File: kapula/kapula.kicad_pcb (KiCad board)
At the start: 4 copper layers, 50 x 59 mm, 161 parts, among them J1 Conn_02x10_Odd_Even, J12 U.FL, J13 U.FL, J3 Conn_02x10_Odd_Even, J4 Conn_ARM_JTAG_SWD_10, J5 U.FL, J9 U.FL, Q1 AO3401A, Q2 AO3401A, Q3 AO3400A, Q4 BSS84, Q5 AO3400A, Q6 AO3400A, T1 BW21S7511A01TF, T2 BW21S7511A01TF, T3 BW21S7511A01TF, T4 BW21S7511A01TF, U1 XC6206P332MR, U2 TP4054, U3 DW01+G, U5 EFR32FG14P233F256GM48-B, U6 XA213-G4J, X1 DSB221SDN, Y1 32768 Hz

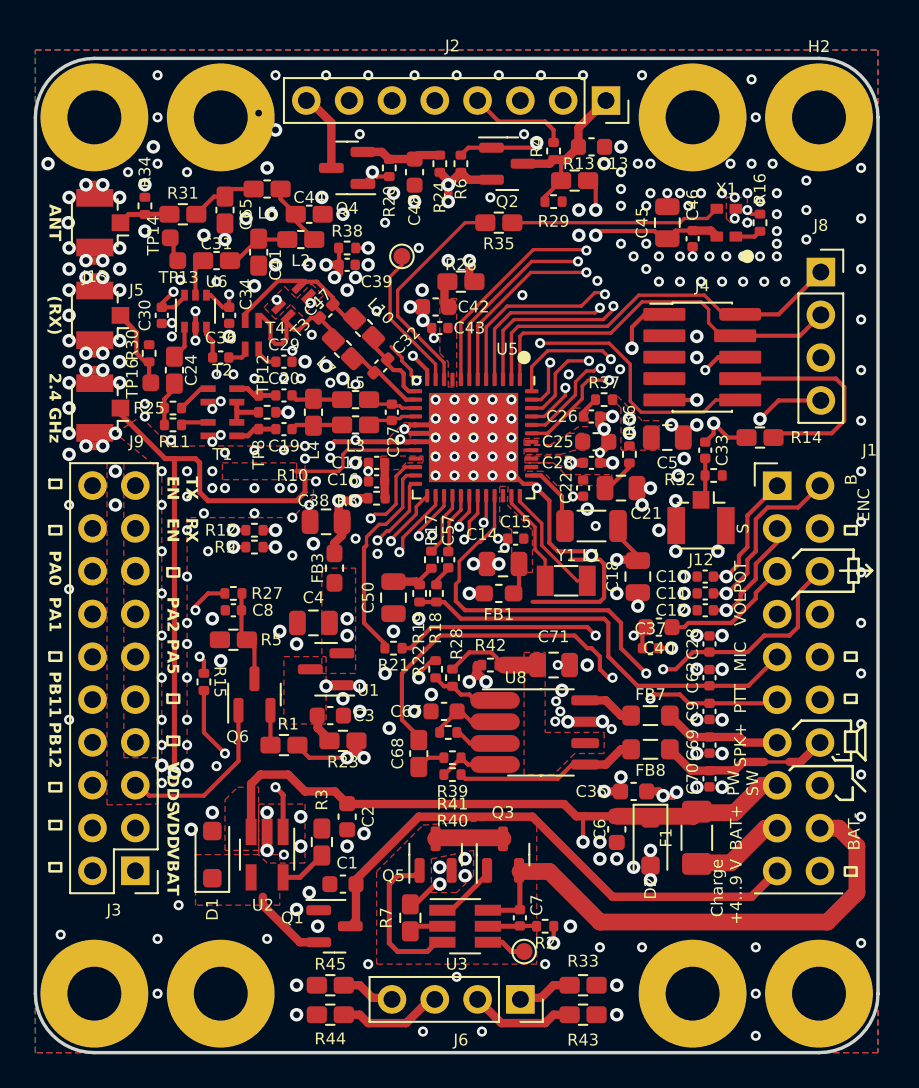
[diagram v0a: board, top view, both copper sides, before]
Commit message: PCB: Add more silkscreen texts, some other fixes
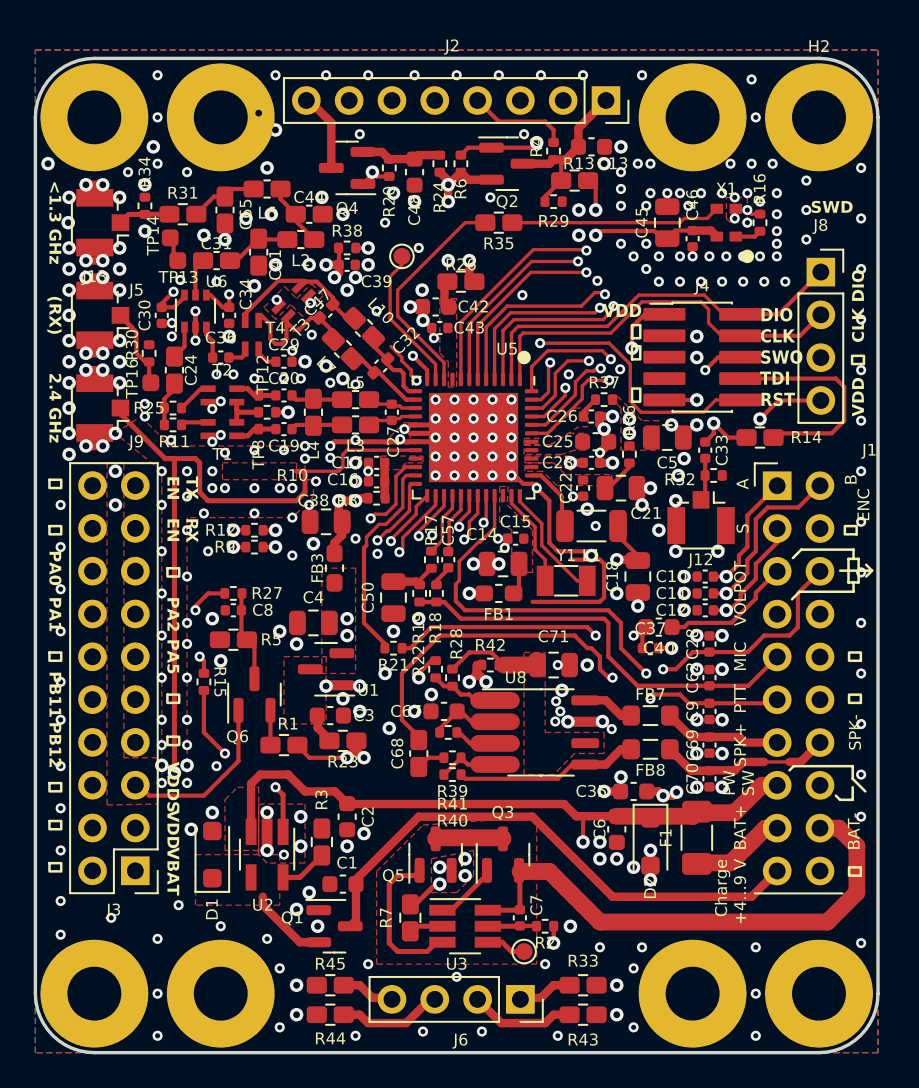
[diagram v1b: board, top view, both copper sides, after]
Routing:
- net GND: vias 368 -> 384
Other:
- board text added: "<1.3 GHz"
- board text added: "DIO CLK SWO TDI RST"
- board text added: "SPK-"
- board text added: "SWD"
- board text added: "VDD ⏚ CLK DIO"
- board text added: "VDD ⏚ ⏚ ⏚"
- board text removed: "ANT"

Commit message: PCB: Small circuit changes and layout improvements
* Add pads for extra series resistor for backlight
* Improve 2nd harmonic rejection of lowpass filter
* Move some components and vias a bit
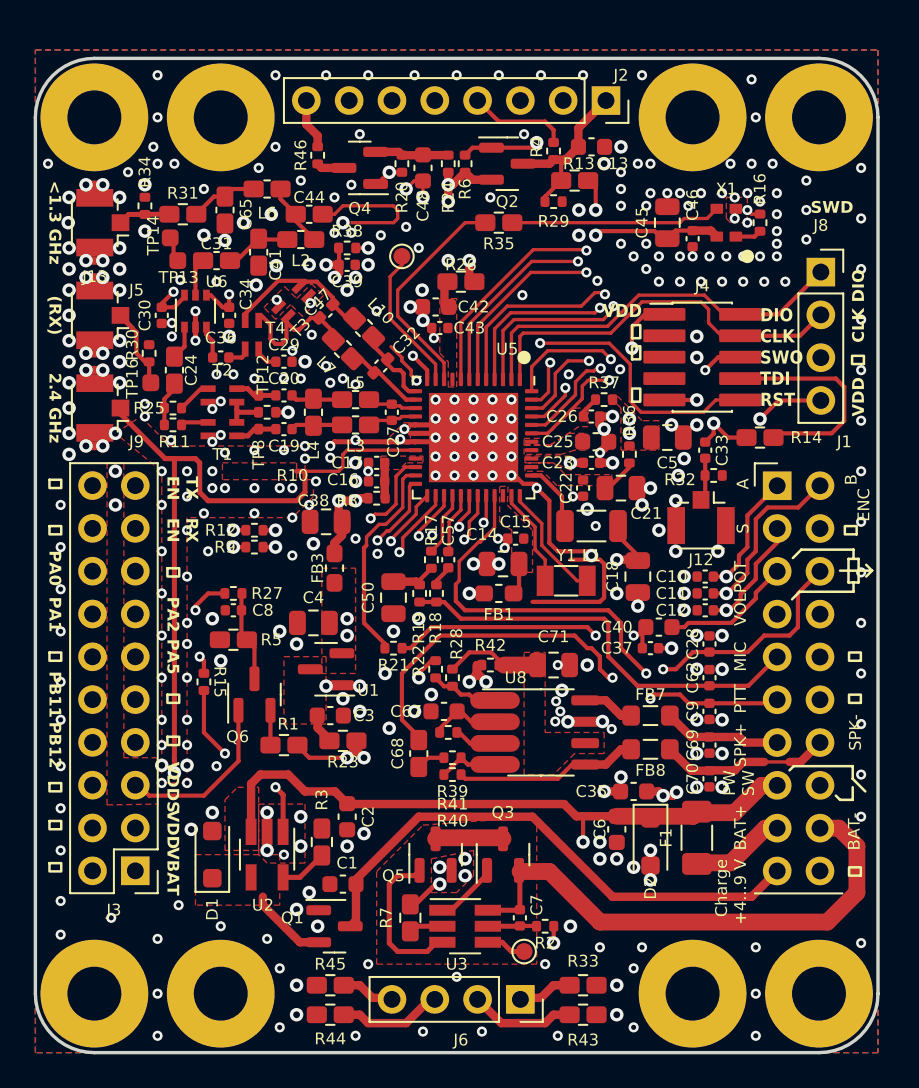
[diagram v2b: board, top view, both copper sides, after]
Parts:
- added NT2: ~, kapula:NetTie-2_SMD_Pad0.2mm, F.Cu at (119.0, 67.2)
- added R46: 0, Resistor_SMD:R_0402_1005Metric, F.Cu at (116.8, 63.2)
- C44: value 10p -> 8p2
- moved R20 0.79 mm to (121.8, 63.8)
- moved Q4 0.75 mm to (119.2, 64.0)
- moved C48 0.56 mm to (123.0, 64.0)
- moved R24 0.50 mm to (124.5, 63.8)
- moved R6 0.25 mm to (125.5, 63.8)
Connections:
- C44 pad 2: GND -> Net-(C44-Pad2)
- Q4 pad 3: /D_LED -> Net-(Q4-D)
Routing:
- net Net-(C44-Pad2): track 0.00 -> 7.61 mm
- net GND: track 66.6 -> 68.7 mm, vias 384 -> 389
- net Net-(Q4-D): track 0.00 -> 1.66 mm
- net /D_LED: track 4.71 -> 3.19 mm
- net /~{D_LED_EN}: track 26.3 -> 25.2 mm

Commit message: PCB: Fix inductor value in lowpass filter
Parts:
- L2, L6: value 22n -> 18n
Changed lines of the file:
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@@
     (descr "Inductor SMD 0603 (1608 Metric), square (rectangular) end terminal, IPC_7351 nominal with elongated pad for handsoldering. (Body size source: http://www.tortai-tech.com/upload/download/2011102023233369053.pdf), generated with kicad-footprint-generator")
     (tags "inductor handsolder")
-    (property "LCSC" "C12099")
+    (property "LCSC" "C48590")
     (property "Sheetfile" "kapula.kicad_sch")
     (property "Sheetname" "")
@@
         (effects (font (size 0.7 0.7) (thickness 0.15)))
     )
-    (fp_text value "22n" (at 0 1.43) (layer "F.Fab")
+    (fp_text value "18n" (at 0 1.43) (layer "F.Fab")
         (effects (font (size 1 1) (thickness 0.15)))
     )
@@
     (descr "Inductor SMD 0603 (1608 Metric), square (rectangular) end terminal, IPC_7351 nominal with elongated pad for handsoldering. (Body size source: http://www.tortai-tech.com/upload/download/2011102023233369053.pdf), generated with kicad-footprint-generator")
     (tags "inductor handsolder")
-    (property "LCSC" "C12099")
+    (property "LCSC" "C48590")
     (property "Sheetfile" "kapula.kicad_sch")
     (property "Sheetname" "")
@@
         (effects (font (size 0.7 0.7) (thickness 0.15)))
     )
-    (fp_text value "22n" (at 0 1.43) (layer "F.Fab")
-        (effects (font (size 1 1) (thickness 0.15)))
-    )
+    (fp_text value "18n" (at 0 1.43) (layer "F.Fab")
+        (effects (font (size 1 1) (thickness 0.15)))
+    )

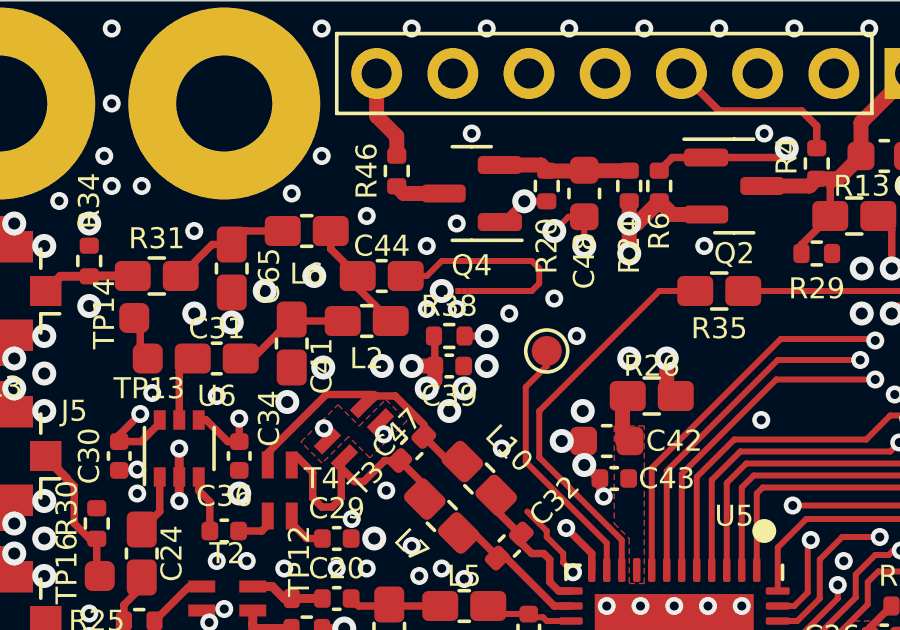
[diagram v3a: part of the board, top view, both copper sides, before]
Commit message: PCB: Modify lowpass to use inductors from JLC basic series
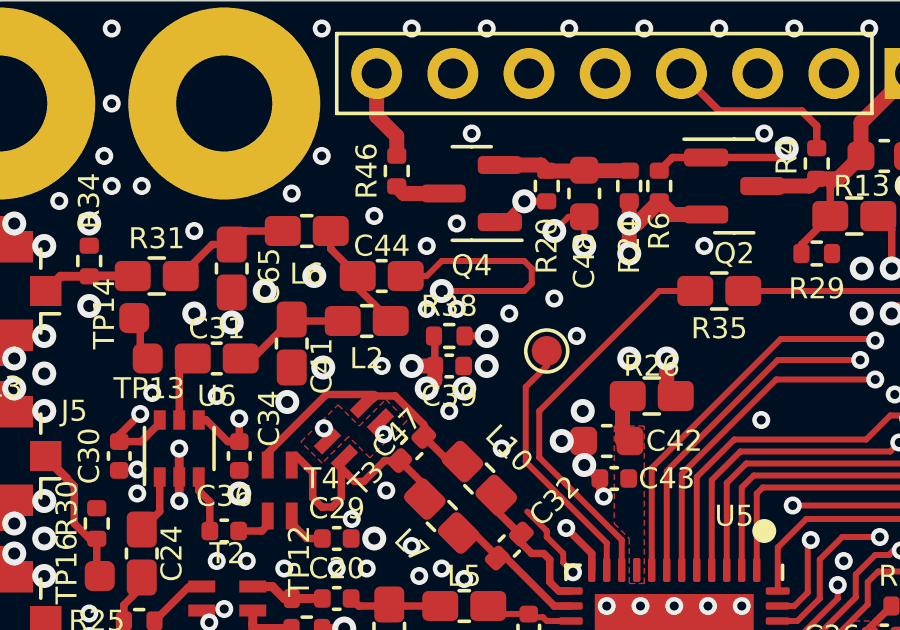
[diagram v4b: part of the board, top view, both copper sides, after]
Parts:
- C41, C65: value 4p7 -> 6p8
- C44: value 8p2 -> 10p
- L2, L6: value 18n -> 15n
- moved NT2 0.25 mm to (118.8, 67.2)
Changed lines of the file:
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@@
     (descr "Inductor SMD 0603 (1608 Metric), square (rectangular) end terminal, IPC_7351 nominal with elongated pad for handsoldering. (Body size source: http://www.tortai-tech.com/upload/download/2011102023233369053.pdf), generated with kicad-footprint-generator")
     (tags "inductor handsolder")
-    (property "LCSC" "C48590")
+    (property "LCSC" "C27143")
     (property "Sheetfile" "kapula.kicad_sch")
     (property "Sheetname" "")
@@
         (effects (font (size 0.7 0.7) (thickness 0.15)))
     )
-    (fp_text value "18n" (at 0 1.43) (layer "F.Fab")
+    (fp_text value "15n" (at 0 1.43) (layer "F.Fab")
         (effects (font (size 1 1) (thickness 0.15)))
     )
@@
     (descr "Inductor SMD 0603 (1608 Metric), square (rectangular) end terminal, IPC_7351 nominal with elongated pad for handsoldering. (Body size source: http://www.tortai-tech.com/upload/download/2011102023233369053.pdf), generated with kicad-footprint-generator")
     (tags "inductor handsolder")
-    (property "LCSC" "C48590")
+    (property "LCSC" "C27143")
     (property "Sheetfile" "kapula.kicad_sch")
     (property "Sheetname" "")
@@
         (effects (font (size 0.7 0.7) (thickness 0.15)))
     )
-    (fp_text value "18n" (at 0 1.43) (layer "F.Fab")
+    (fp_text value "15n" (at 0 1.43) (layer "F.Fab")
         (effects (font (size 1 1) (thickness 0.15)))
     )
@@
     (descr "Capacitor SMD 0603 (1608 Metric), square (rectangular) end terminal, IPC_7351 nominal with elongated pad for handsoldering. (Body size source: IPC-SM-782 page 76, https://www.pcb-3d.com/wordpress/wp-content/uploads/ipc-sm-782a_amendment_1_and_2.pdf), generated with kicad-footprint-generator")
     (tags "capacitor handsolder")
-    (property "LCSC" "C1569")
+    (property "LCSC" "C1679")
     (property "Sheetfile" "kapula.kicad_sch")
     (property "Sheetname" "")
@@
         (effects (font (size 0.7 0.7) (thickness 0.15)))
     )
-    (fp_text value "4p7" (at 0 1.43 90) (layer "F.Fab")
+    (fp_text value "6p8" (at 0 1.43 90) (layer "F.Fab")
         (effects (font (size 1 1) (thickness 0.15)))
     )
@@
     (descr "Capacitor SMD 0603 (1608 Metric), square (rectangular) end terminal, IPC_7351 nominal with elongated pad for handsoldering. (Body size source: IPC-SM-782 page 76, https://www.pcb-3d.com/wordpress/wp-content/uploads/ipc-sm-782a_amendment_1_and_2.pdf), generated with kicad-footprint-generator")
     (tags "capacitor handsolder")
-    (property "LCSC" "C1569")
+    (property "LCSC" "C1679")
     (property "Sheetfile" "kapula.kicad_sch")
     (property "Sheetname" "")
@@
         (effects (font (size 0.7 0.7) (thickness 0.15)))
     )
-    (fp_text value "4p7" (at 0 1.43 90) (layer "F.Fab")
+    (fp_text value "6p8" (at 0 1.43 90) (layer "F.Fab")
         (effects (font (size 1 1) (thickness 0.15)))
     )
@@
   )
   (footprint "kapula:NetTie-2_SMD_Pad0.2mm" (layer "F.Cu")
-    (at 119 67.25 180)
+    (at 118.75 67.25 180)
     (descr "Net tie, 2 pin, 0.5mm square SMD pads")
     (tags "net tie")
@@
     (descr "Capacitor SMD 0603 (1608 Metric), square (rectangular) end terminal, IPC_7351 nominal with elongated pad for handsoldering. (Body size source: IPC-SM-782 page 76, https://www.pcb-3d.com/wordpress/wp-content/uploads/ipc-sm-782a_amendment_1_and_2.pdf), generated with kicad-footprint-generator")
     (tags "capacitor handsolder")
-    (property "LCSC" "C1685")
+    (property "LCSC" "C1634")
     (property "Sheetfile" "kapula.kicad_sch")
     (property "Sheetname" "")
@@
         (effects (font (size 0.7 0.7) (thickness 0.15)))
     )
-    (fp_text value "8p2" (at 0 1.43) (layer "F.Fab")
+    (fp_text value "10p" (at 0 1.43) (layer "F.Fab")
         (effects (font (size 1 1) (thickness 0.15)))
     )
@@
   (via (at 114.75 76.5) (size 0.6) (drill 0.3) (layers "F.Cu" "B.Cu") (free) (net 2))
   (via (at 140 69.25) (size 0.6) (drill 0.3) (layers "F.Cu" "B.Cu") (free) (net 2))
-  (via (at 116.25 69.75) (size 0.8) (drill 0.4) (layers "F.Cu" "B.Cu") (free) (net 2))
+  (via (at 116.25 69.75) (size 0.6) (drill 0.3) (layers "F.Cu" "B.Cu") (free) (net 2))
   (via (at 134.7 75.95) (size 0.6) (drill 0.3) (layers "F.Cu" "B.Cu") (free) (net 2))
   (via (at 136 58.5) (size 0.6) (drill 0.3) (layers "F.Cu" "B.Cu") (free) (net 2))
@@
   (via (at 143.75 63.75) (size 0.6) (drill 0.3) (layers "F.Cu" "B.Cu") (free) (net 2))
   (via (at 119 76.85) (size 0.6) (drill 0.3) (layers "F.Cu" "B.Cu") (free) (net 2))
-  (via (at 118.5 71.25) (size 0.8) (drill 0.4) (layers "F.Cu" "B.Cu") (free) (net 2))
+  (via (at 118.5 71.25) (size 0.6) (drill 0.3) (layers "F.Cu" "B.Cu") (free) (net 2))
   (via (at 110.25 86.75) (size 0.6) (drill 0.3) (layers "F.Cu" "B.Cu") (free) (net 2))
   (via (at 136.25 68.5) (size 0.6) (drill 0.3) (layers "F.Cu" "B.Cu") (free) (net 2))
@@
   (via (at 119 70.5) (size 0.8) (drill 0.4) (layers "F.Cu" "B.Cu") (free) (net 2))
   (via (at 134.75 100.15) (size 0.8) (drill 0.4) (layers "F.Cu" "B.Cu") (free) (net 2))
-  (via (at 115.75 64.75) (size 0.6) (drill 0.3) (layers "F.Cu" "B.Cu") (free) (net 2))
+  (via (at 116 64.75) (size 0.6) (drill 0.3) (layers "F.Cu" "B.Cu") (free) (net 2))
   (via (at 139.5 65.5) (size 0.6) (drill 0.3) (layers "F.Cu" "B.Cu") (free) (net 2))
   (via (at 111 93.25) (size 0.8) (drill 0.4) (layers "F.Cu" "B.Cu") (free) (net 2))
@@
   (segment (start 116.99 64) (end 118.3125 64) (width 0.5) (layer "F.Cu") (net 119))
   (segment (start 116.75 63.76) (end 116.99 64) (width 0.5) (layer "F.Cu") (net 119))
-  (segment (start 117.05 66.75) (end 117.75 66.75) (width 0.2) (layer "F.Cu") (net 120))
-  (segment (start 121.25 67.25) (end 121.5 67) (width 0.2) (layer "F.Cu") (net 120))
-  (segment (start 121.5 66.5) (end 121.5 67) (width 0.2) (layer "F.Cu") (net 120))
-  (segment (start 119.25 67.25) (end 121.25 67.25) (width 0.2) (layer "F.Cu") (net 120))
-  (segment (start 121.25 66.25) (end 121.5 66.5) (width 0.2) (layer "F.Cu") (net 120))
-  (segment (start 118.25 66.25) (end 121.25 66.25) (width 0.2) (layer "F.Cu") (net 120))
-  (segment (start 117.75 66.75) (end 118.25 66.25) (width 0.2) (layer "F.Cu") (net 120))
+  (segment (start 118.25 66.25) (end 117.75 66.75) (width 0.2) (layer "F.Cu") (net 120))
+  (segment (start 118.95 67.25) (end 121 67.25) (width 0.2) (layer "F.Cu") (net 120))
+  (segment (start 121 67.25) (end 121.25 67) (width 0.2) (layer "F.Cu") (net 120))
+  (segment (start 121.25 67) (end 121.25 66.5) (width 0.2) (layer "F.Cu") (net 120))
+  (segment (start 117.75 66.75) (end 117.05 66.75) (width 0.2) (layer "F.Cu") (net 120))
+  (segment (start 121 66.25) (end 118.25 66.25) (width 0.2) (layer "F.Cu") (net 120))
+  (segment (start 121.25 66.5) (end 121 66.25) (width 0.2) (layer "F.Cu") (net 120))
   (zone (net 48) (net_name "/BC_VCC") (layer "F.Cu") (hatch edge 0.508)
     (priority 1)
@@
     (polygon
       (pts
-        (xy 116.65 71.8)
-        (xy 116.65 72.15)
+        (xy 116.75 71.75)
+        (xy 116.75 72.15)
         (xy 116.45 72.35)
         (xy 116.15 72.35)
-        (xy 114.25 72.15)
-        (xy 114.05 72.05)
-        (xy 114 71.8)
-        (xy 114.1 71.55)
+        (xy 114.25 72.25)
+        (xy 113.95 72.1)
+        (xy 113.9 71.8)
+        (xy 114 71.6)
         (xy 116.75 70)
         (xy 116.75 69.25)
